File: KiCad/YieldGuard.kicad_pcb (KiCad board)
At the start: 2 copper layers, 55 x 60 mm, 4 parts, among them J1 Conn_01x04_Socket, U1 ESP32-DEVKITC, U2 HX711

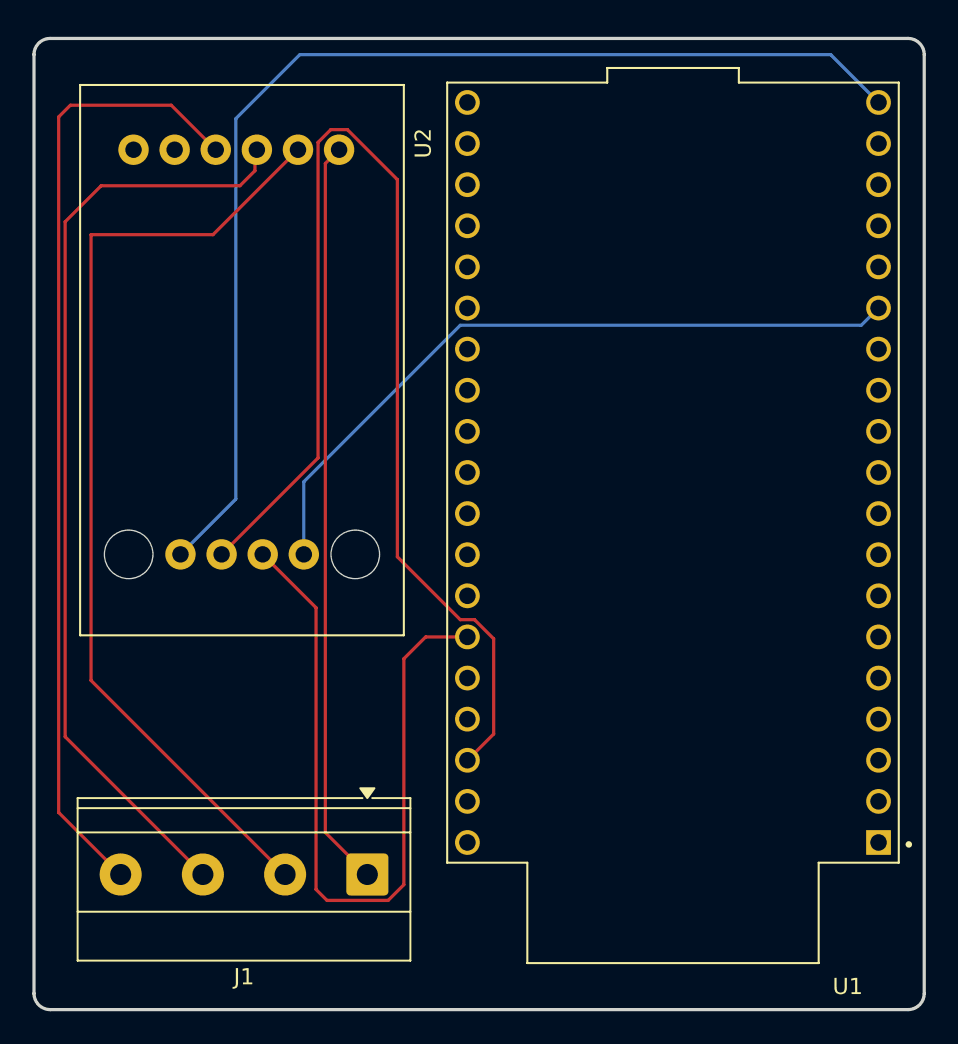
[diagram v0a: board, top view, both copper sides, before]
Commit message: fixed the dimension of screw terminal of load cell
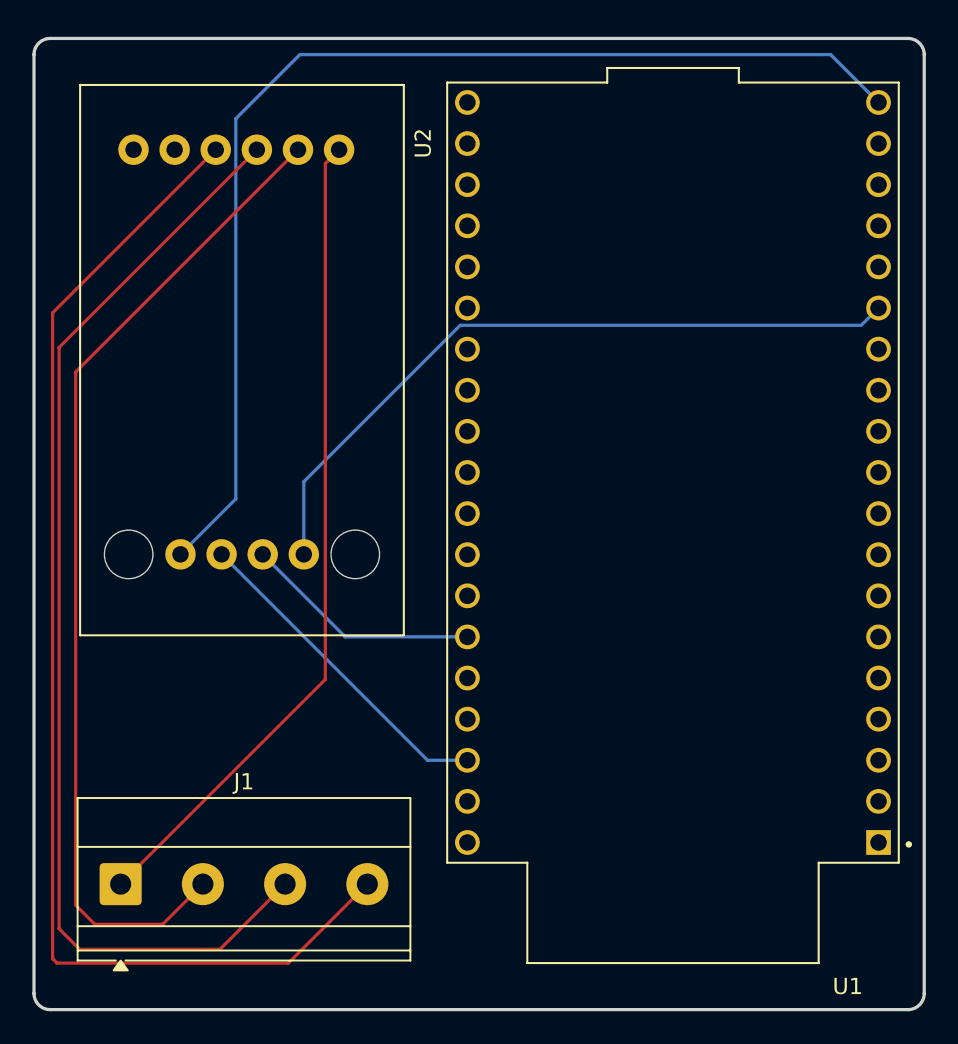
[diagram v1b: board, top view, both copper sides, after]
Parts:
- moved J1 15.3 mm to (110.0, 91.7), turned to 0 degrees
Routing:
- net /CLOCK: track 74.0 -> 20.5 mm
- net /DATA: track 46.6 -> 14.8 mm
- net /GREEN_WIRE: track 59.5 -> 75.7 mm
- net /WHITE_WIRE: track 58.2 -> 69.3 mm
- net /RED_WIRE_PWR: track 46.2 -> 51.0 mm
- net /BLACK_WIRE_GND: track 59.5 -> 61.7 mm

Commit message: Bit changes in PCB and Schematic and Completed BoM
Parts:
- U1: value ESP32-DEVKITC -> ESP32_C3_Super_Mini; footprint KiCad:MODULE_ESP32-DEVKITC -> KiCad:ESP32-C3_SuperMini
- moved J1 32.0 mm to (136.2, 73.4)
- moved G*** 26.9 mm to (114.3, 56.4)
- moved U1 12.7 mm to (143.7, 53.6), turned to 0 degrees
- moved U2 1.17 mm to (118.3, 58.5)
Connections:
- U1 pad 1: unconnected-(U1-3V3-Pad1) -> /5V
- U1 pad 14: /GND -> unconnected-(U1-GPIO10-Pad14)
- U1 pad 2: unconnected-(U1-EN-Pad2) -> /GND
- U1 pad 4: unconnected-(U1-SENSOR_VN-Pad4) -> /DATA
- U1 pad 9: unconnected-(U1-IO25-Pad9) -> /CLOCK
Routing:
- net /GREEN_WIRE: track 75.7 -> 0.00 mm
- net /5V: track 70.9 -> 0.00 mm
- net /WHITE_WIRE: track 69.3 -> 0.00 mm
- net /BLACK_WIRE_GND: track 61.7 -> 0.00 mm
- net /RED_WIRE_PWR: track 51.0 -> 0.00 mm
- net /GND: track 44.4 -> 0.00 mm
- net /CLOCK: track 20.5 -> 0.00 mm
- net /DATA: track 14.8 -> 0.00 mm
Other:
- board size 55 x 60 mm -> 50 x 40 mm
- board text removed: "Designed by Safeer Hassan :)"

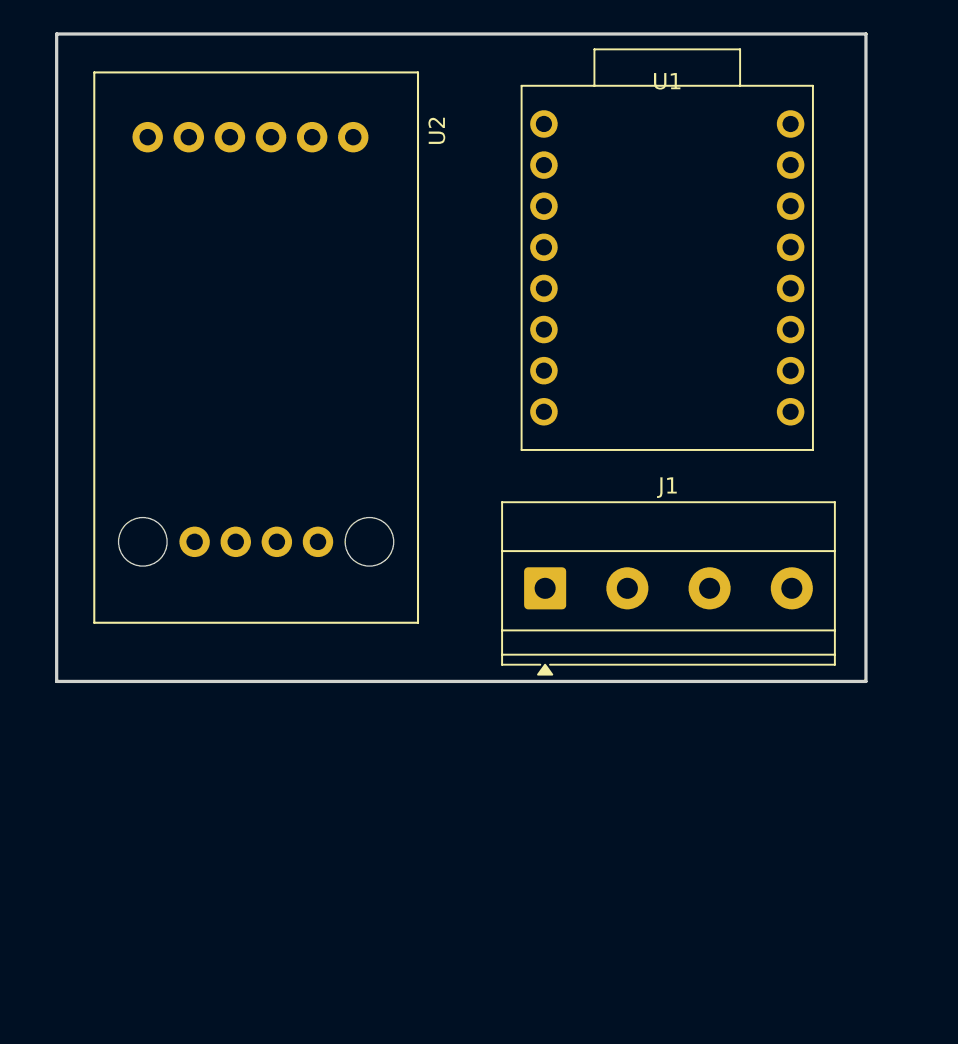
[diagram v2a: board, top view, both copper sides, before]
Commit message: routed updated PCB
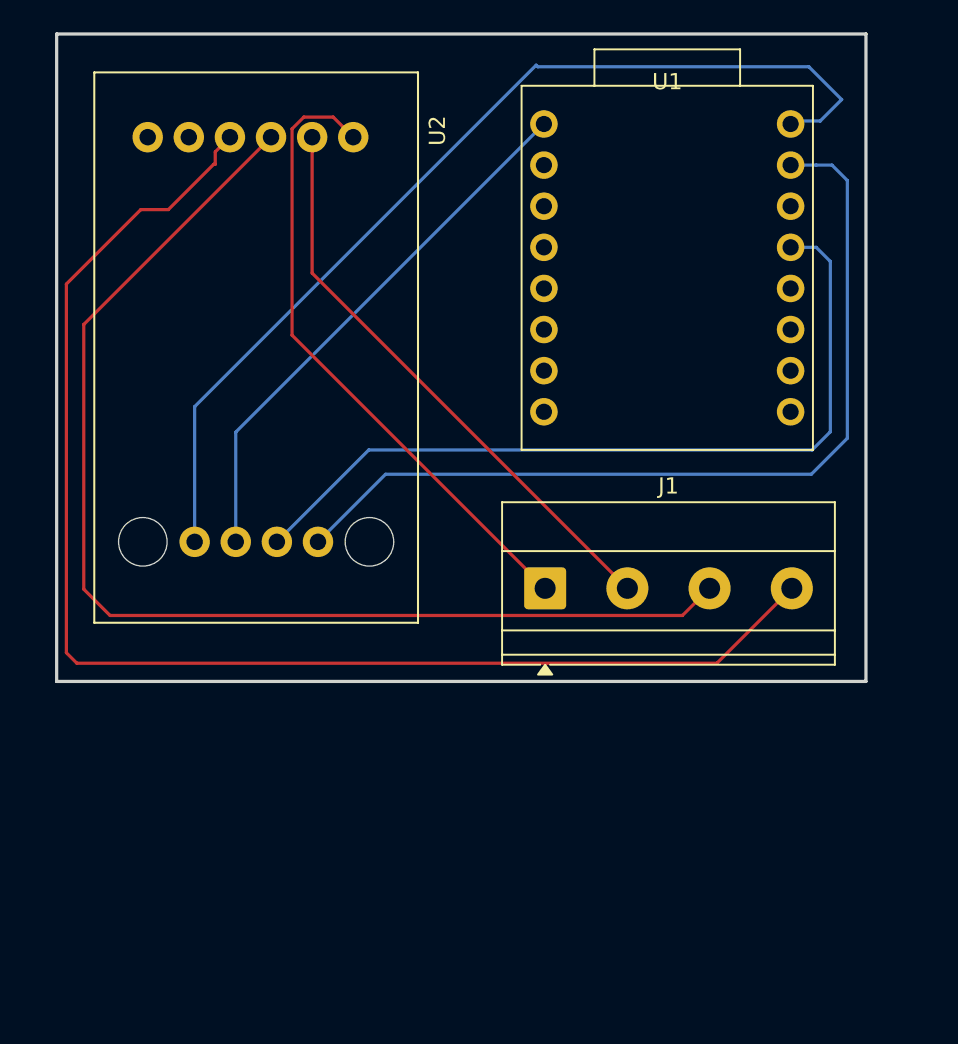
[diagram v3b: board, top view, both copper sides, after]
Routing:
- net /GREEN_WIRE: track 0.00 -> 84.1 mm
- net /WHITE_WIRE: track 0.00 -> 72.8 mm
- net /5V: track 0.00 -> 61.7 mm
- net /GND: track 0.00 -> 55.2 mm
- net /DATA: track 0.00 -> 50.4 mm
- net /RED_WIRE_PWR: track 0.00 -> 39.5 mm
- net /BLACK_WIRE_GND: track 0.00 -> 35.9 mm
- net /CLOCK: track 0.00 -> 33.7 mm
